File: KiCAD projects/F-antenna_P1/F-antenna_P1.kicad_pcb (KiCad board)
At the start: 2 copper layers, 71.1 x 134.6 mm, 1 part, among them J1 MMCX_Connector

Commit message: PCB Changes
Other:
- outline, holes or cut-outs redrawn
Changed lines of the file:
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@@
 	)
 	(gr_line
-		(start 133.35 95.25)
+		(start 133.35 104.14)
 		(end 88.9 50.8)
 		(stroke
@@
 	(gr_line
 		(start 133.35 146.05)
-		(end 133.35 95.25)
+		(end 133.35 104.14)
 		(stroke
 			(width 0.05)
@@
 			(keep_text_aligned yes)
 		)
-		(gr_text "1.75"
+		(gr_text "1750"
 			(at 111.125 156.33 0)
 			(layer "User.2")
@@
 			(keep_text_aligned yes)
 		)
-		(gr_text "0.5125"
+		(gr_text "512.5"
 			(at 76.955 114.14125 90)
 			(layer "User.2")
@@
 			(keep_text_aligned yes)
 		)
-		(gr_text "0.75"
+		(gr_text "750"
 			(at 76.955 73.025 90)
 			(layer "User.2")
@@
 			(keep_text_aligned yes)
 		)
-		(gr_text "0.625"
+		(gr_text "625"
 			(at 80.9625 46.475 0)
 			(layer "User.2")
@@
 			(keep_text_aligned yes)
 		)
-		(gr_text "0.45"
+		(gr_text "450"
 			(at 72.39 36.95 0)
 			(layer "User.2")
@@
 			(keep_text_aligned yes)
 		)
-		(gr_text "0.75"
+		(gr_text "750"
 			(at 76.955 130.175 90)
 			(layer "User.2")
@@
 			(keep_text_aligned yes)
 		)
-		(gr_text "4"
+		(gr_text "4000"
 			(at 56 101.6 90)
 			(layer "User.2")
@@
 			(keep_text_aligned yes)
 		)
-		(gr_text "1"
+		(gr_text "1000"
 			(at 78.105 55.245 90)
 			(layer "User.2")

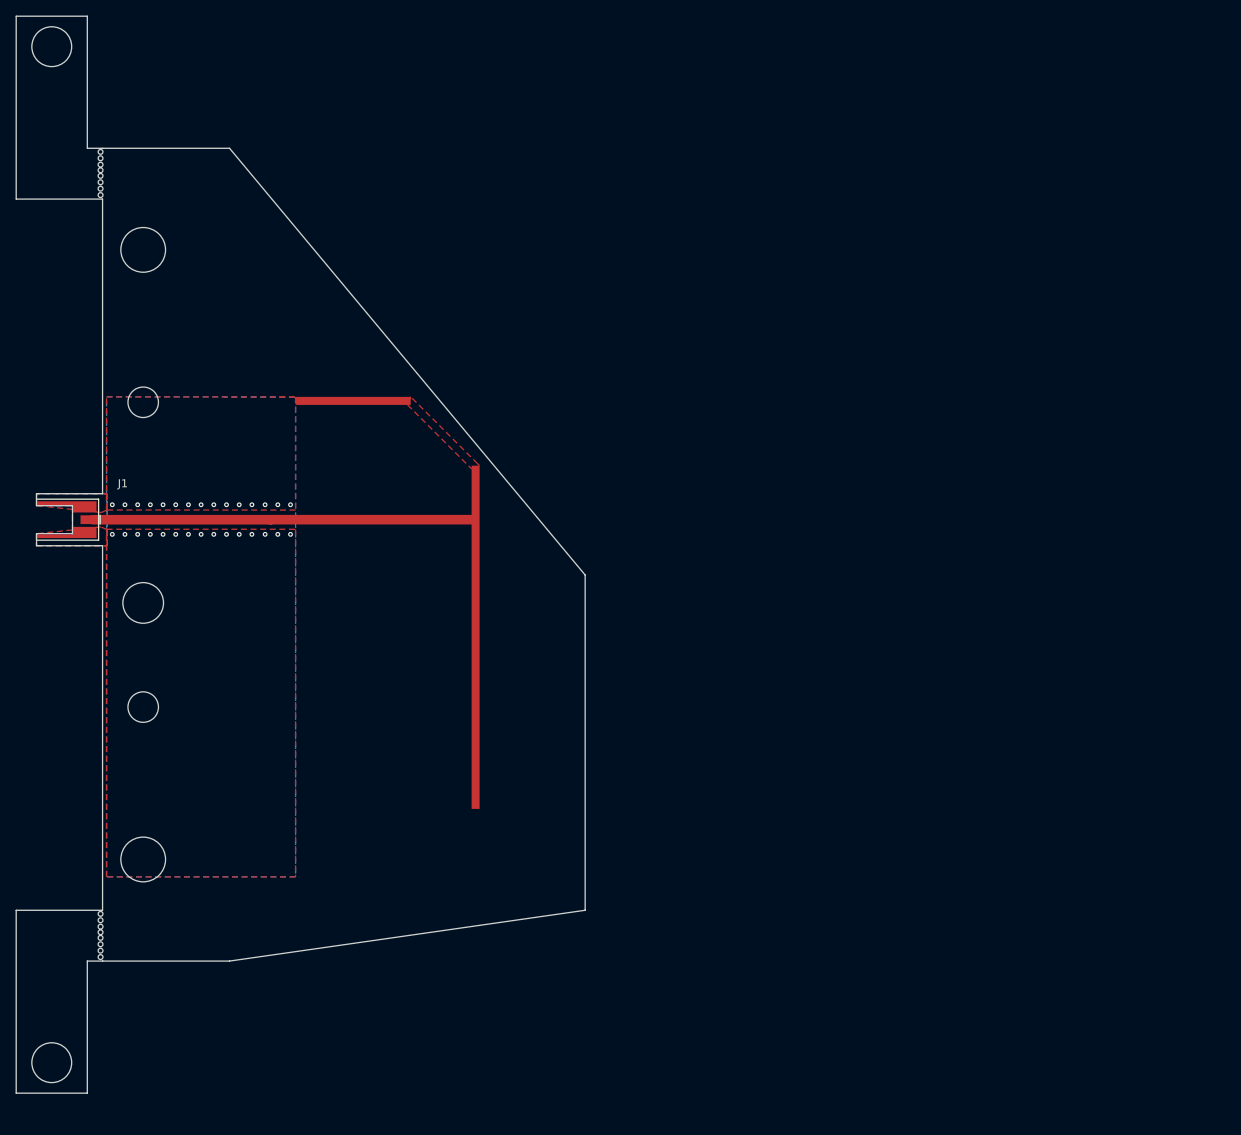
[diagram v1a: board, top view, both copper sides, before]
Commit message: Updated PCB files
The PCB files now have the more optimized geometry and reinforced mounting for production
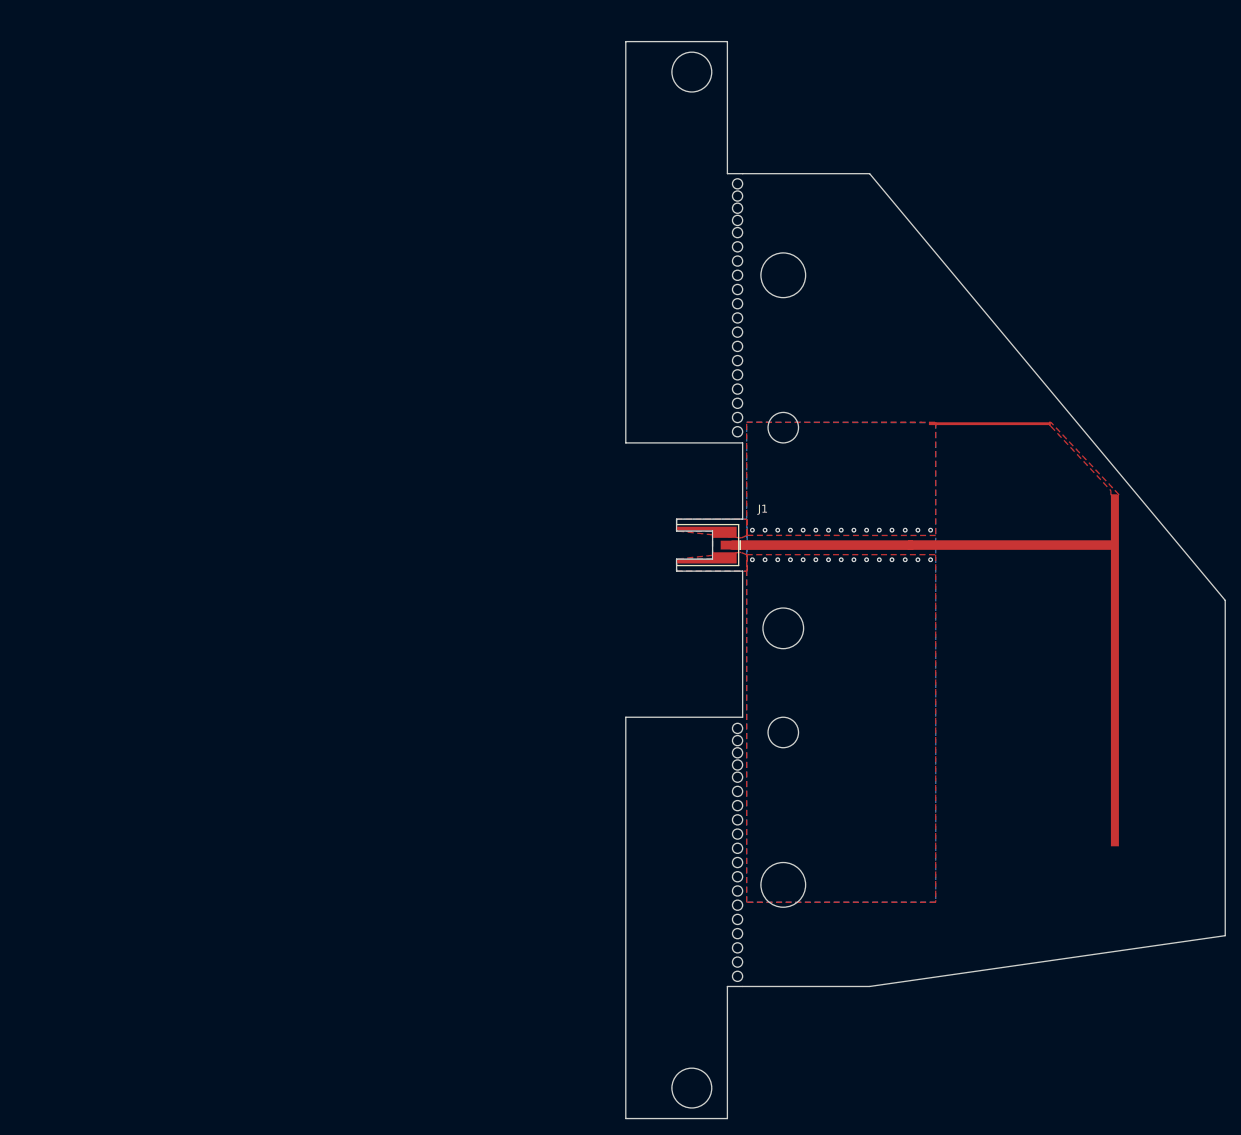
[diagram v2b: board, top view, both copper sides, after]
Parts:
- moved J1 80.1 mm to (148.5, 100.4)
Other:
- board size 71.1 x 134.6 mm -> 74.9 x 134.6 mm
